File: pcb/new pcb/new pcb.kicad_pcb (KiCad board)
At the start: 2 copper layers, 66.3 x 71.8 mm, 44 parts, among them J1 Lidar conector, J10 Conn_01x04, J11 Conn_01x04, J12 Conn_01x04, J13 Conn_01x04, J14 Conn_01x04, J15 Conn_01x04, J2 RJ9, J3 I2C quiic conector, J5 Conn_01x04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

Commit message: fix the pcb
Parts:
- added R12: 100, Resistor_SMD:R_1206_3216Metric_Pad1.30x1.75mm_HandSolder, F.Cu at (183.0, 88.5)
- added R13: 100, Resistor_SMD:R_1206_3216Metric_Pad1.30x1.75mm_HandSolder, F.Cu at (183.0, 83.5)
- renumbered debug to debug1
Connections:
- debug1 pad 1: Net-(A1-SWDIO) -> Net-(A1-SWCLK)
- debug1 pad 3: Net-(A1-SWCLK) -> Net-(A1-SWDIO)
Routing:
- net Net-(A1-SWDIO): track 32.9 -> 64.5 mm
- net Net-(A1-SWCLK): track 37.5 -> 58.8 mm
- net GND: vias 55 -> 57

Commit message: actual fix
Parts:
- removed R12, R13: 100, Resistor_SMD:R_1206_3216Metric_Pad1.30x1.75mm_HandSolder
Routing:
- net Net-(A1-SWDIO): track 64.5 -> 36.1 mm
- net Net-(A1-SWCLK): track 58.8 -> 35.1 mm
- net GND: vias 57 -> 55

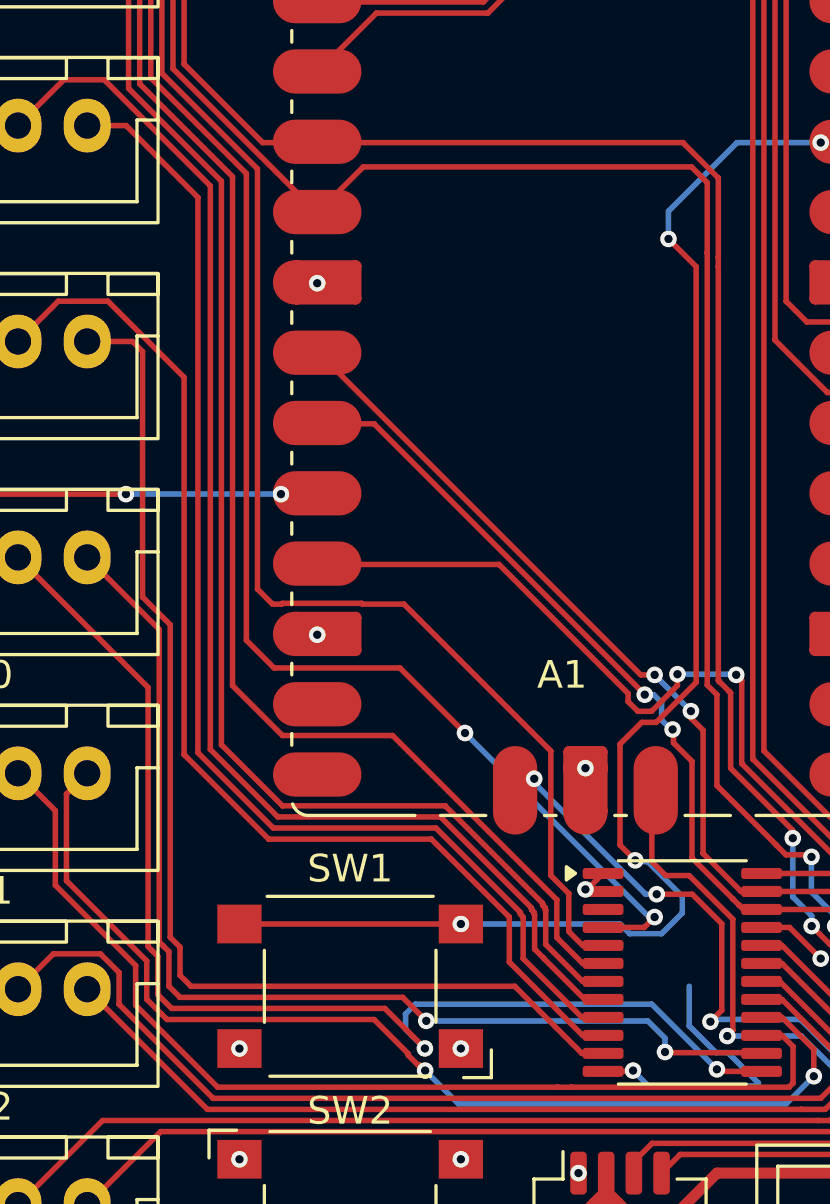
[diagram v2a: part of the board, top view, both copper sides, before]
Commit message: added reset to gpio14
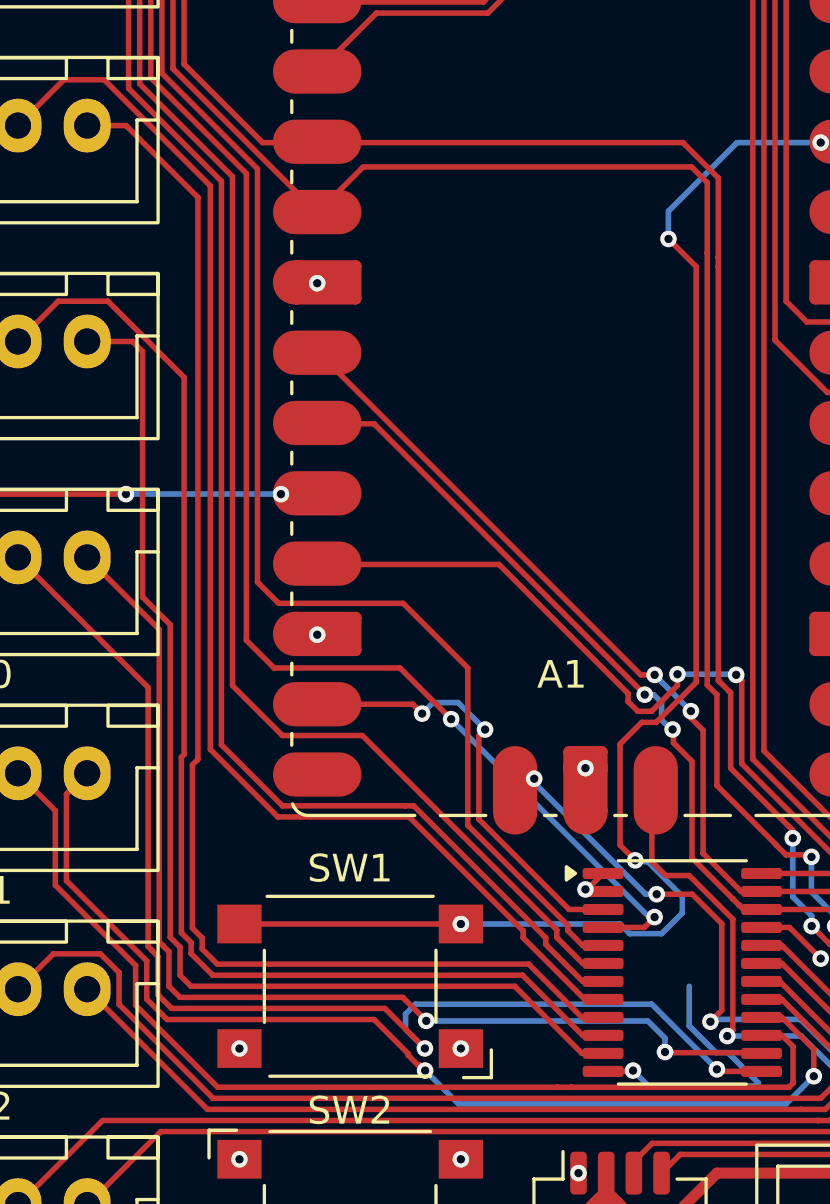
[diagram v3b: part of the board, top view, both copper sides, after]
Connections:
- A1 pad 19: unconnected-(A1-GPIO14-Pad19) -> Net-(A1-GPIO14)
- U3 pad 3: unconnected-(U3-~{RESET}-Pad3) -> Net-(A1-GPIO14)
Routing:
- net Net-(A1-GPIO14): track 0.00 -> 15.9 mm, vias 0 -> 2
- net Net-(J7-Pin_4): track 44.7 -> 48.0 mm
- net Net-(J8-Pin_3): track 41.7 -> 44.9 mm
- net Net-(J6-Pin_4): track 50.3 -> 49.7 mm
- net Net-(J7-Pin_3): track 48.3 -> 47.7 mm
- net Net-(J6-Pin_3): track 54.0 -> 53.4 mm
